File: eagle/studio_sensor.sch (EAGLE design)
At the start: 9 parts

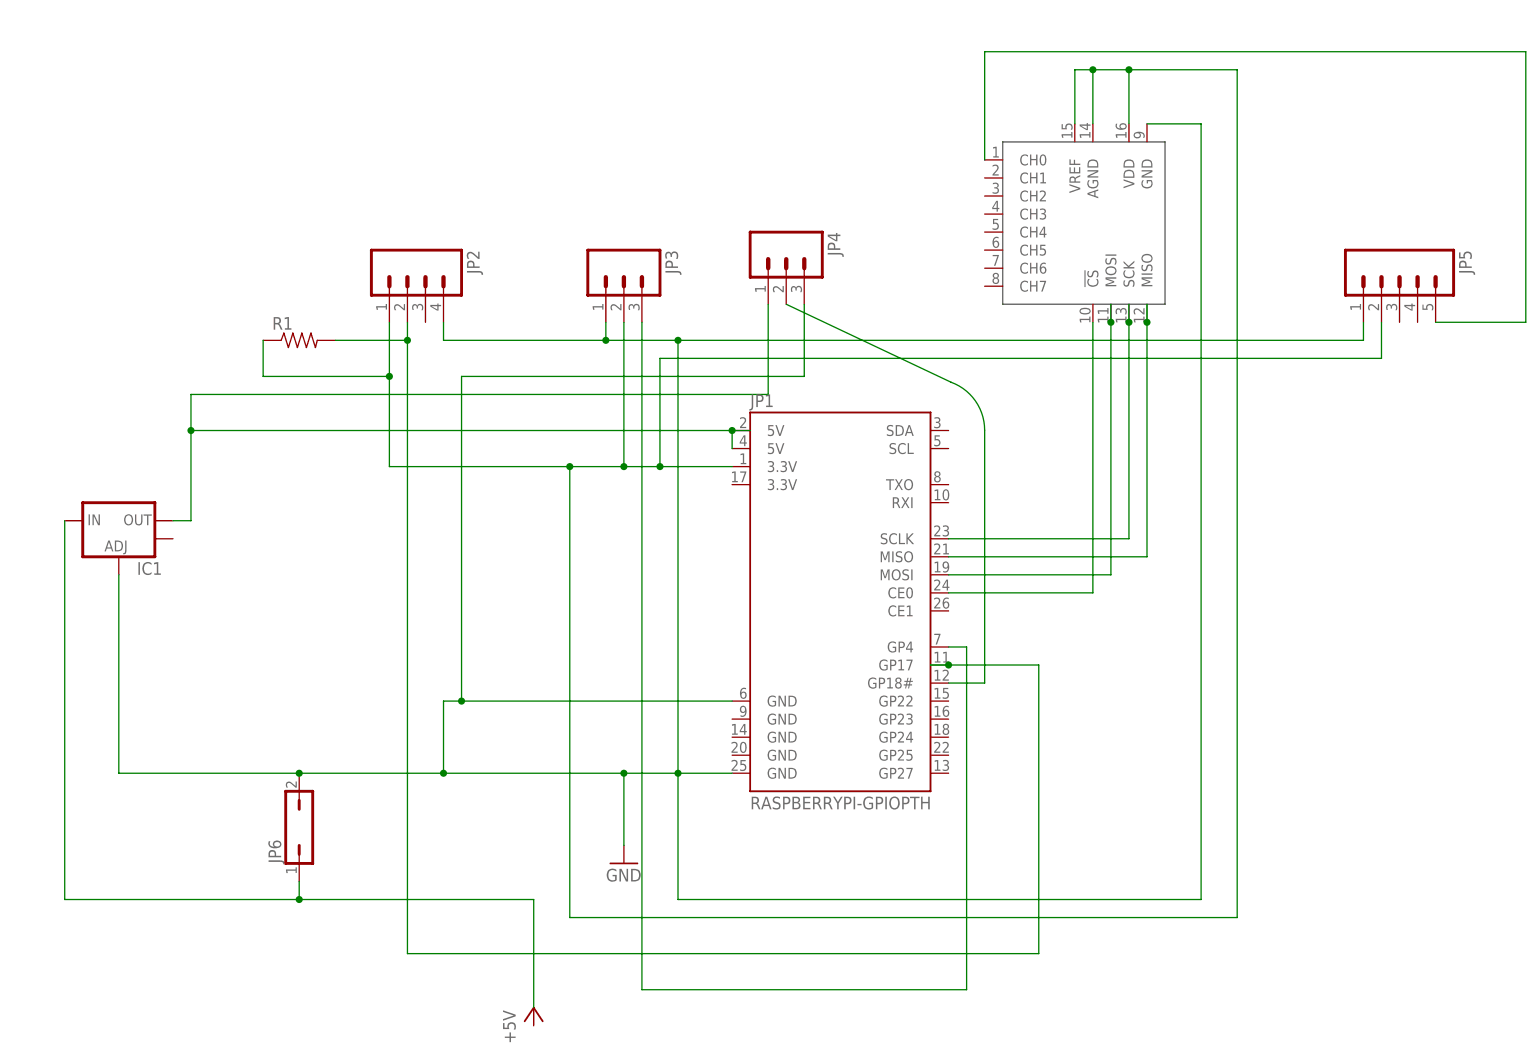
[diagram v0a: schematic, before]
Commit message: updating studio sensors
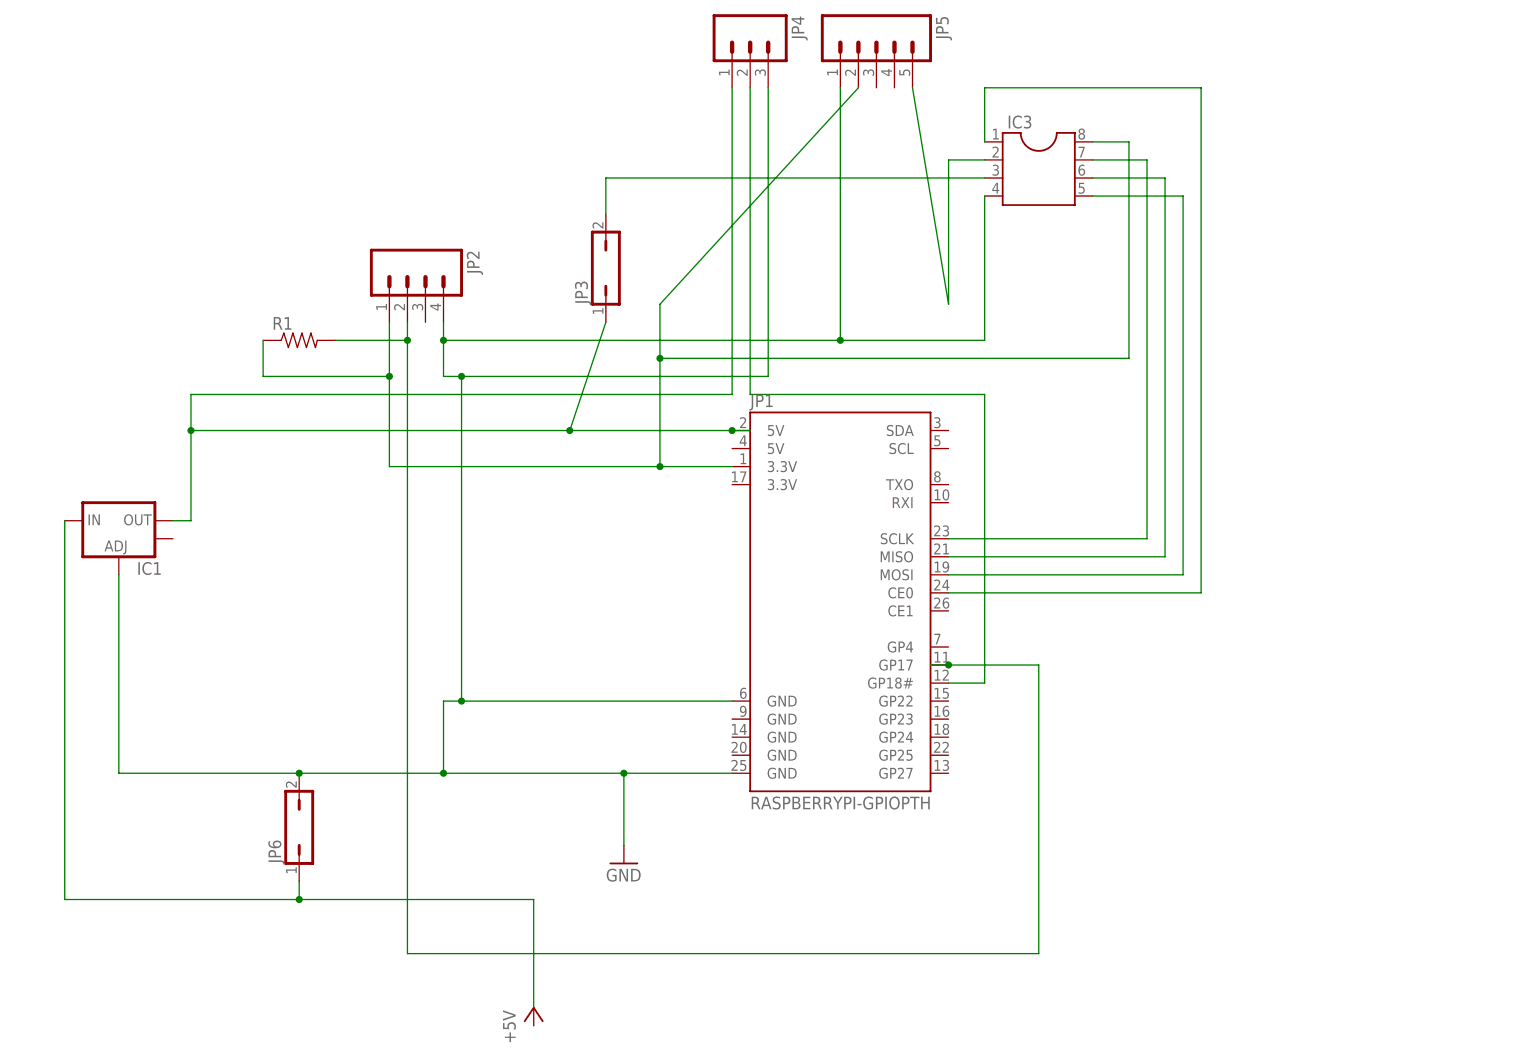
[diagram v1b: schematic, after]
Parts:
- removed U$1: MCP3008SL, MCP3008:MCP3008SL
- added IC3: (no value), ic-package:DIL8S
- JP3: device SparkFun-Connectors:M03PTH -> jumper:JP1Q
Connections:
- removed net N$14: JP1.GP4, JP3.3
- new net N$3: IC3.3, JP3.2
- net GND: now also IC3.4; no longer JP3.1, U$1.GND
- net N$1: now also JP1.5V@2, JP3.1; no longer JP1.5V@4
- net N$2: now also IC3.8; no longer JP3.2, U$1.AGND, U$1.VDD, U$1.VREF
- net N$4: now also IC3.7; no longer U$1.SCK
- net N$5: now also IC3.6; no longer U$1.MISO
- net N$6: now also IC3.5; no longer U$1.MOSI
- net N$7: now also IC3.1; no longer U$1.!CS
- net N$8: now also IC3.2; no longer U$1.CH0
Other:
- moved on the sheet: JP4, JP5

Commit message: redoing DB
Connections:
- net GND: now also JP4.2; no longer JP4.3
- net N$13: now also JP4.3; no longer JP4.2
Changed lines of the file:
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@@
 <wire x1="5.08" y1="20.32" x2="5.08" y2="30.48" width="0.1524" layer="91"/>
 <wire x1="5.08" y1="30.48" x2="7.62" y2="30.48" width="0.1524" layer="91"/>
-<pinref part="JP4" gate="G$1" pin="3"/>
 <wire x1="7.62" y1="30.48" x2="45.72" y2="30.48" width="0.1524" layer="91"/>
-<wire x1="50.8" y1="116.84" x2="50.8" y2="76.2" width="0.1524" layer="91"/>
-<wire x1="50.8" y1="76.2" x2="7.62" y2="76.2" width="0.1524" layer="91"/>
+<wire x1="48.26" y1="76.2" x2="7.62" y2="76.2" width="0.1524" layer="91"/>
 <wire x1="7.62" y1="76.2" x2="7.62" y2="30.48" width="0.1524" layer="91"/>
 <junction x="7.62" y="30.48"/>
@@
 <wire x1="5.08" y1="76.2" x2="7.62" y2="76.2" width="0.1524" layer="91"/>
 <junction x="7.62" y="76.2"/>
+<pinref part="JP4" gate="G$1" pin="2"/>
+<wire x1="48.26" y1="116.84" x2="48.26" y2="76.2" width="0.1524" layer="91"/>
 </segment>
 </net>
@@
 <wire x1="81.28" y1="73.66" x2="81.28" y2="33.02" width="0.1524" layer="91"/>
 <wire x1="81.28" y1="33.02" x2="76.2" y2="33.02" width="0.1524" layer="91"/>
-<pinref part="JP4" gate="G$1" pin="2"/>
-<wire x1="48.26" y1="116.84" x2="48.26" y2="73.66" width="0.1524" layer="91"/>
-<wire x1="48.26" y1="73.66" x2="81.28" y2="73.66" width="0.1524" layer="91"/>
+<wire x1="50.8" y1="73.66" x2="81.28" y2="73.66" width="0.1524" layer="91"/>
+<pinref part="JP4" gate="G$1" pin="3"/>
+<wire x1="50.8" y1="73.66" x2="50.8" y2="116.84" width="0.1524" layer="91"/>
 </segment>
 </net>

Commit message: server updates
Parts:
- added C1: (no value), SparkFun-Capacitors:CAP0603-CAP
- added J1: POWER_JACKPTH, SparkFun-Connectors:POWER_JACKPTH
- JP6: device jumper:JP1Q -> jumper:JP2E
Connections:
- new net N$11: C1.2, J1.PWR
- new net N$12: C1.1, JP6.2
- net GND: now also J1.GND; no longer JP6.2
- net N$1: now also JP6.3, R1.2
- net N$10: no longer R1.2
- net N$13: now also R1.1
- net N$2: no longer R1.1
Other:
- moved on the sheet: JP3, JP4, R1
